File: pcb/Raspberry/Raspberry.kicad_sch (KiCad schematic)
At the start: 24 parts, among them J1 +5V, J10 SWCLK, J11 GND, J12 SWDIO, J13 UART_TX, J14 UART_RX, J15 PC1, J16 PC0, J17 PB14, J18 GND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

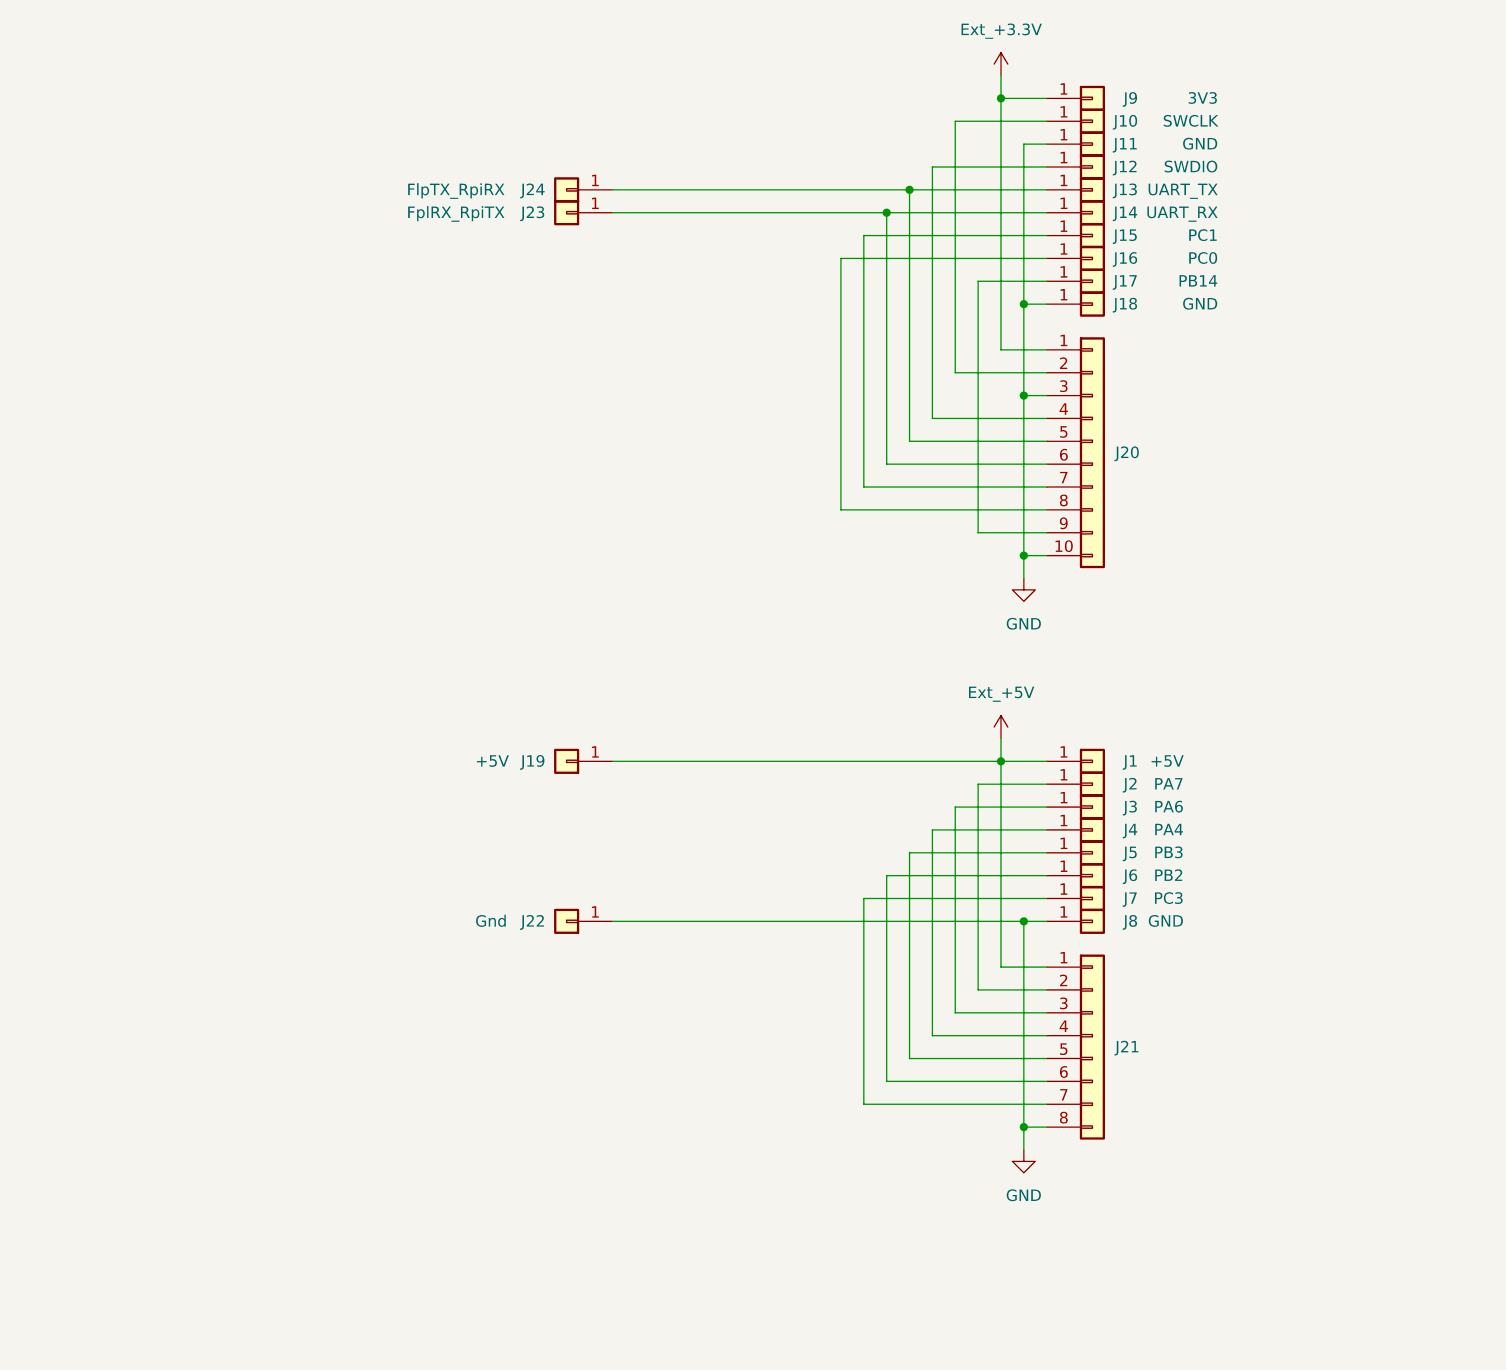
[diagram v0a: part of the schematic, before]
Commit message: [RPI] Draw schematic
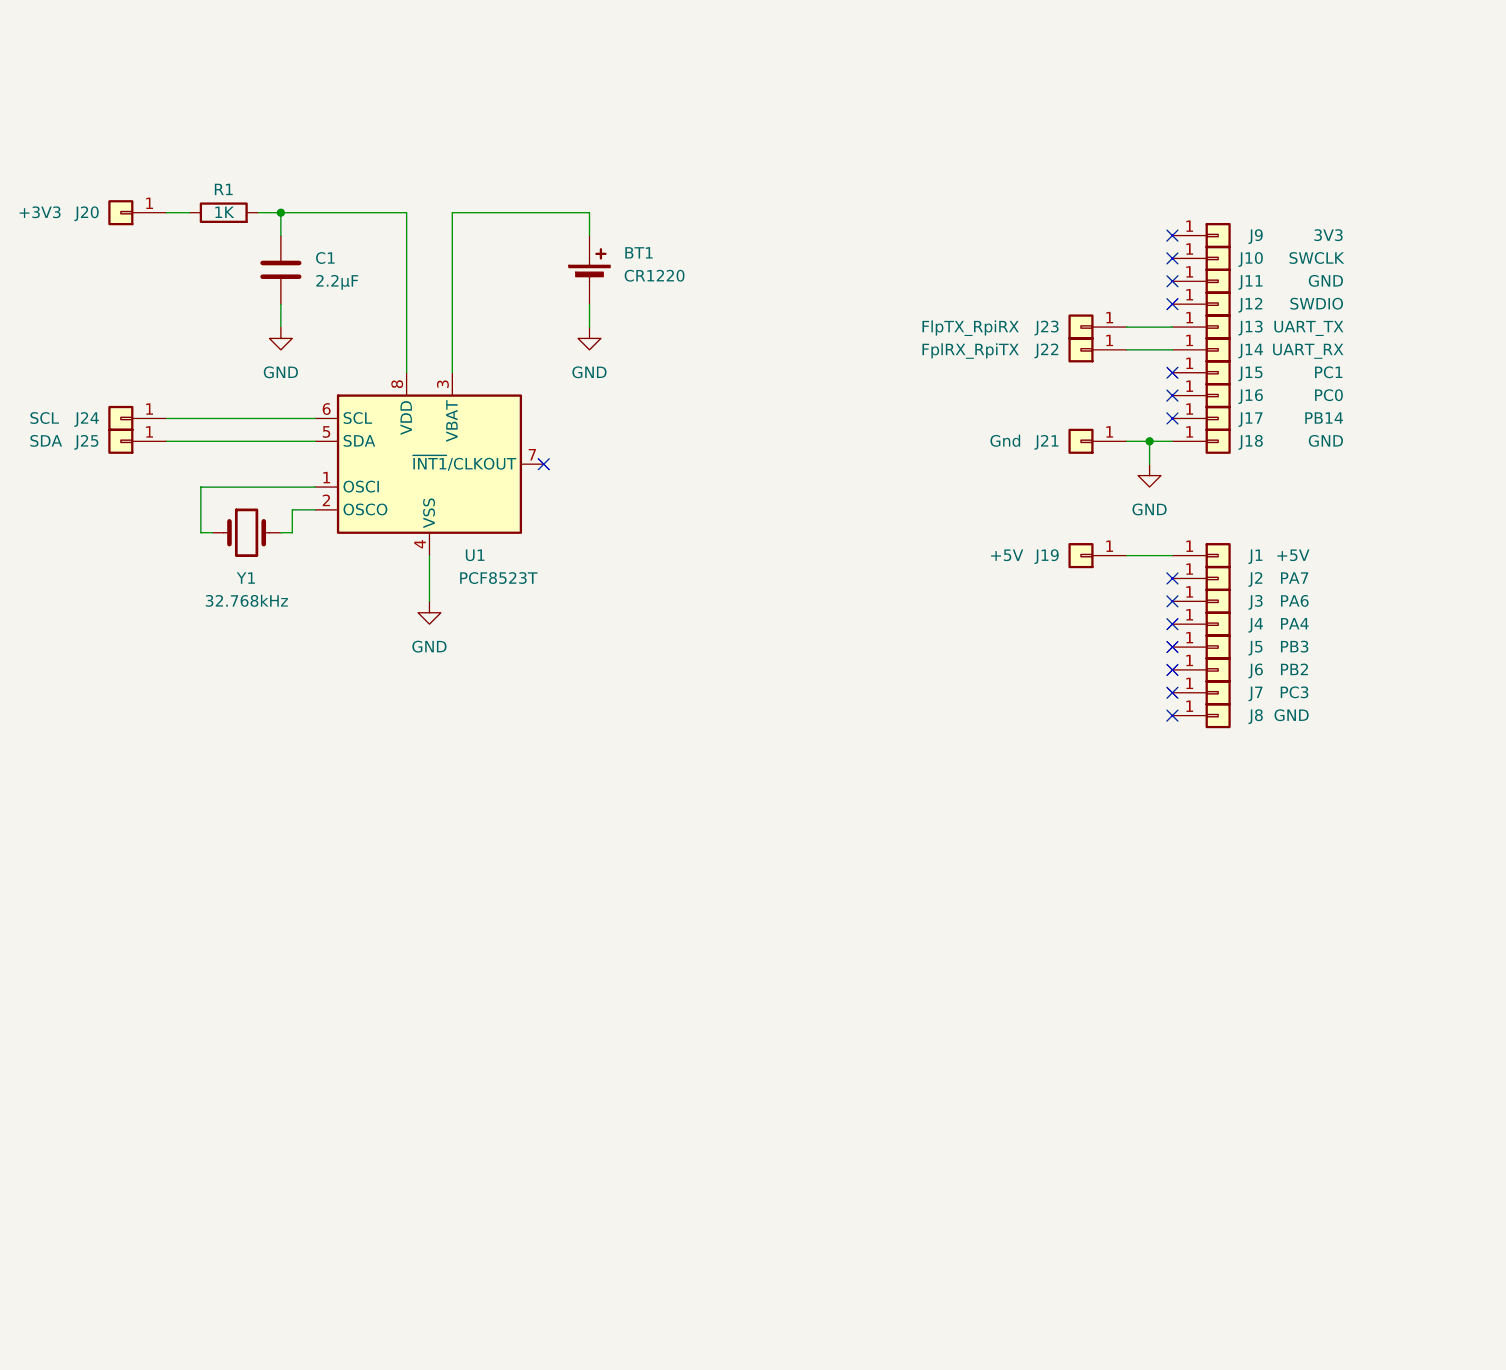
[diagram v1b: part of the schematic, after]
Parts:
- removed J20: Conn_01x10, Connector_PinHeader_2.54mm:PinHeader_1x10_P2.54mm_Vertical, symbol Connector_Generic:Conn_01x10
- removed J21: Conn_01x08, Connector_PinHeader_2.54mm:PinHeader_1x08_P2.54mm_Vertical, symbol Connector_Generic:Conn_01x08
- added BT1: CR1220, MeineBib:Q&J CR1220-2, symbol Device:Battery_Cell
- added C1: 2.2µF, Capacitor_SMD:C_0603_1608Metric, symbol Device:C
- added J20: +3V3, MeineBib:Protopin_Small, symbol Connector_Generic:Conn_01x01
- added J24: SCL, MeineBib:Protopin_Small, symbol Connector_Generic:Conn_01x01
- added J25: SDA, MeineBib:Protopin_Small, symbol Connector_Generic:Conn_01x01
- added R1: 1K, Resistor_SMD:R_0603_1608Metric, symbol Device:R
- added U1: PCF8523T, Package_SO:SOIC-8_3.9x4.9mm_P1.27mm, symbol Timer_RTC:PCF8523T
- added Y1: 32.768kHz, Crystal:Crystal_SMD_3215-2Pin_3.2x1.5mm, symbol Device:Crystal
- J1, J10, J11, J12, J13, J14, J15, J16, J17, J18, J2, J3, J4, J5, J6, J7, J8, J9: now left out of the parts list
- J19: footprint MeineBib:Board-Board-1mmEdge-2,54mm -> MeineBib:Protopin_Small; now left out of the parts list
- J21: renamed from J22; footprint MeineBib:Board-Board-1mmEdge-2,54mm -> MeineBib:Protopin_Small; now left out of the parts list
- J22: renamed from J23; footprint MeineBib:Board-Board-1mmEdge-2,54mm -> MeineBib:Protopin_Small; now left out of the parts list
- J23: renamed from J24; footprint MeineBib:Board-Board-1mmEdge-2,54mm -> MeineBib:Protopin_Small; now left out of the parts list
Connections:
- net GND: now also BT1.2 (-), C1.2, U1.4 (VSS); no longer J11.1 (Pin_1), J8.1 (Pin_1)
- net Ext_+3.3V: no longer names the net of J9.1 (Pin_1)
- net Ext_+5V: no longer names the net of J1.1 (Pin_1), J19.1 (Pin_1)
- new net: BT1.1 (+), U1.3 (VBAT)
- new net: J25.1 (Pin_1), U1.5 (SDA)
- new net: J20.1 (Pin_1), R1.1
- new net: U1.1 (OSCI), Y1.1
- new net: U1.2 (OSCO), Y1.2
- new net: J24.1 (Pin_1), U1.6 (SCL)
- new net: C1.1, R1.2, U1.8 (VDD)
- no-connect marks 0 -> 15
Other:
- moved on the sheet: J1, J10, J11, J12, J13, J14, J15, J16, J17, J18, J19, J2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

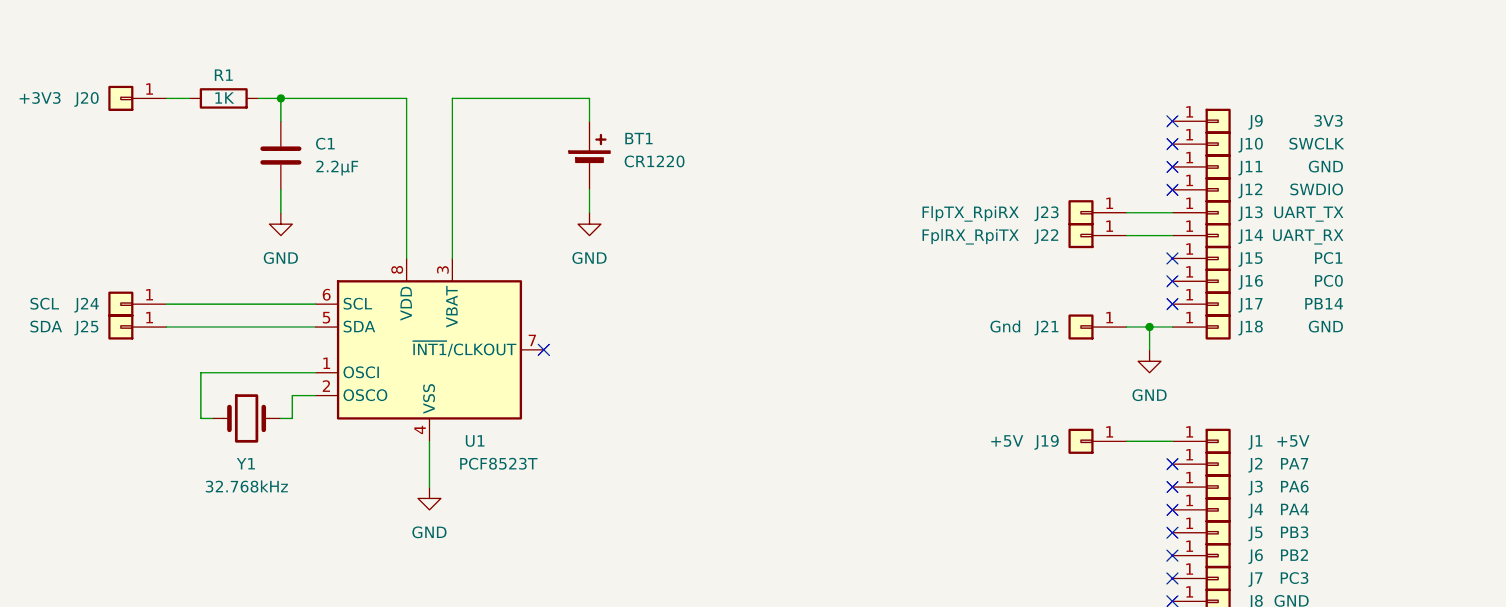
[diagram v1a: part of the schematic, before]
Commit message: [RPI] Route PCB
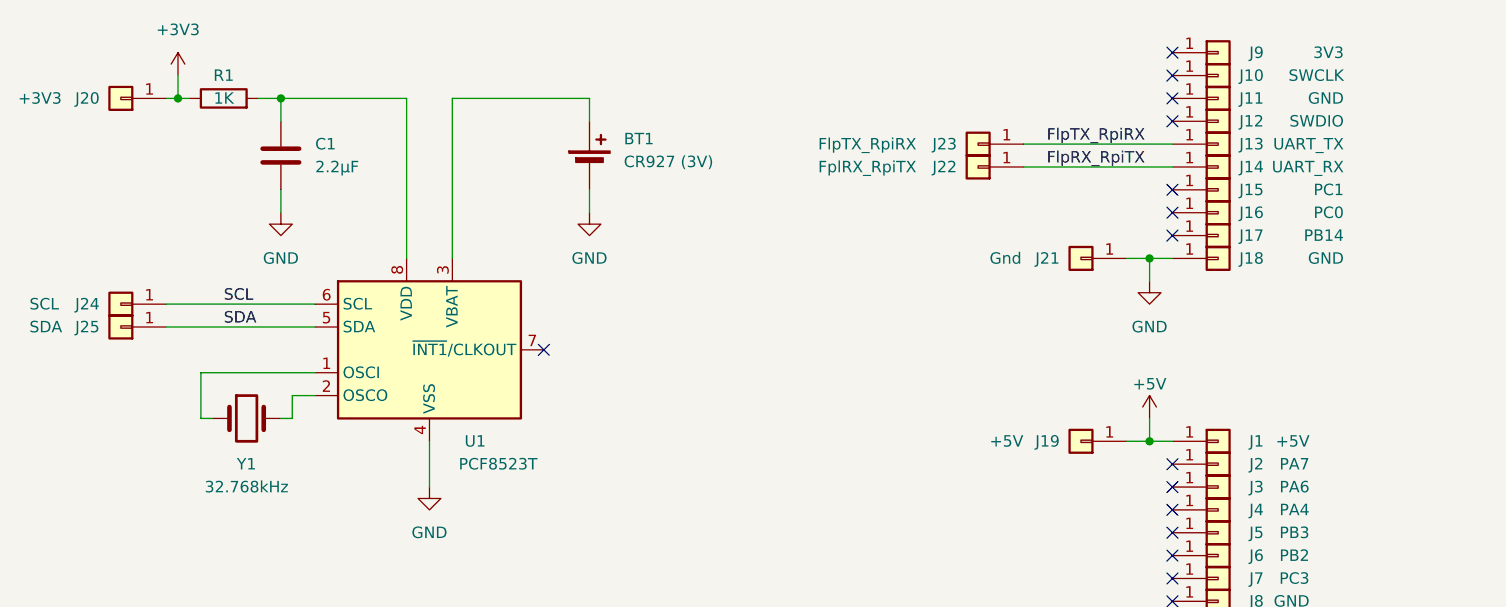
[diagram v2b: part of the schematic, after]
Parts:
- BT1: value CR1220 -> CR927 (3V); footprint MeineBib:Q&J CR1220-2 -> MeineBib:MY-927-01 CR927 Battery Holder; LCSC C70381 -> C964850
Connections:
- net FlpRX_RpiTX: now reaches J14.1 (Pin_1), J22.1 (Pin_1)
- net SDA: now reaches J25.1 (Pin_1), U1.5 (SDA)
- net +3V3: now reaches J20.1 (Pin_1), R1.1
- net SCL: now reaches J24.1 (Pin_1), U1.6 (SCL)
- net FlpTX_RpiRX: now reaches J13.1 (Pin_1), J23.1 (Pin_1)
- net +5V: now reaches J1.1 (Pin_1), J19.1 (Pin_1)
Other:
- moved on the sheet: J10, J11, J12, J13, J14, J15, J16, J17, J18, J21, J22, J23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

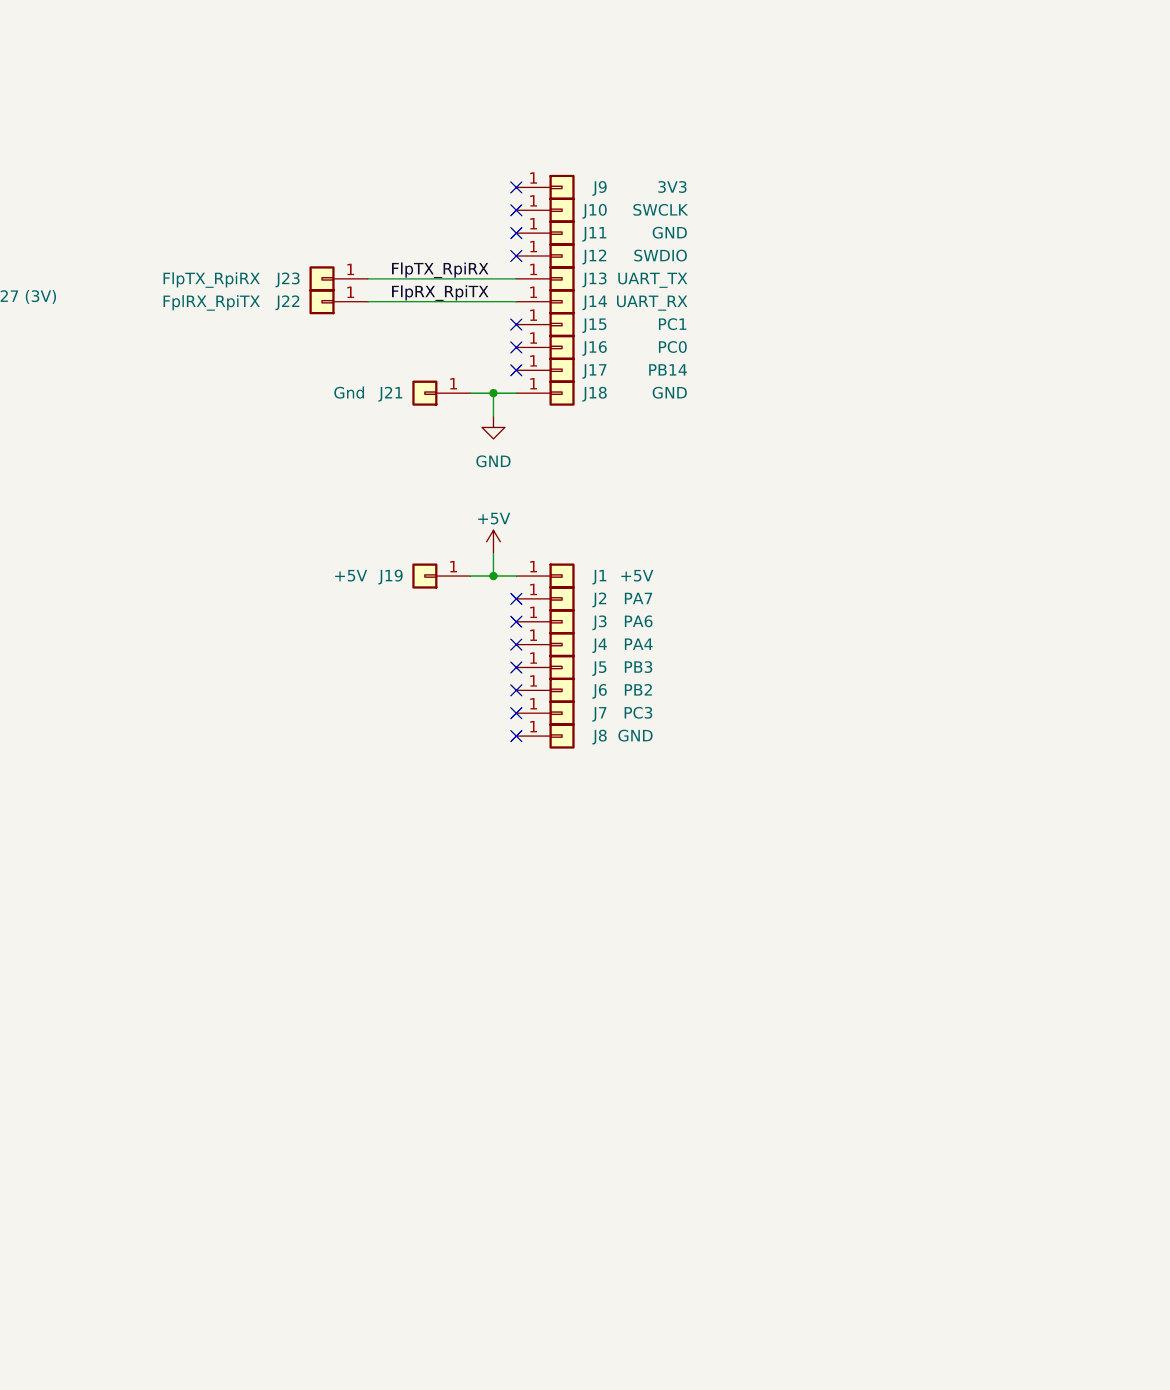
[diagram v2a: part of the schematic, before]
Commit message: [RPI] Fix PCB not actually connected to Flipper
- Added previously removed headers that act as mandatory vias from one side to the other.
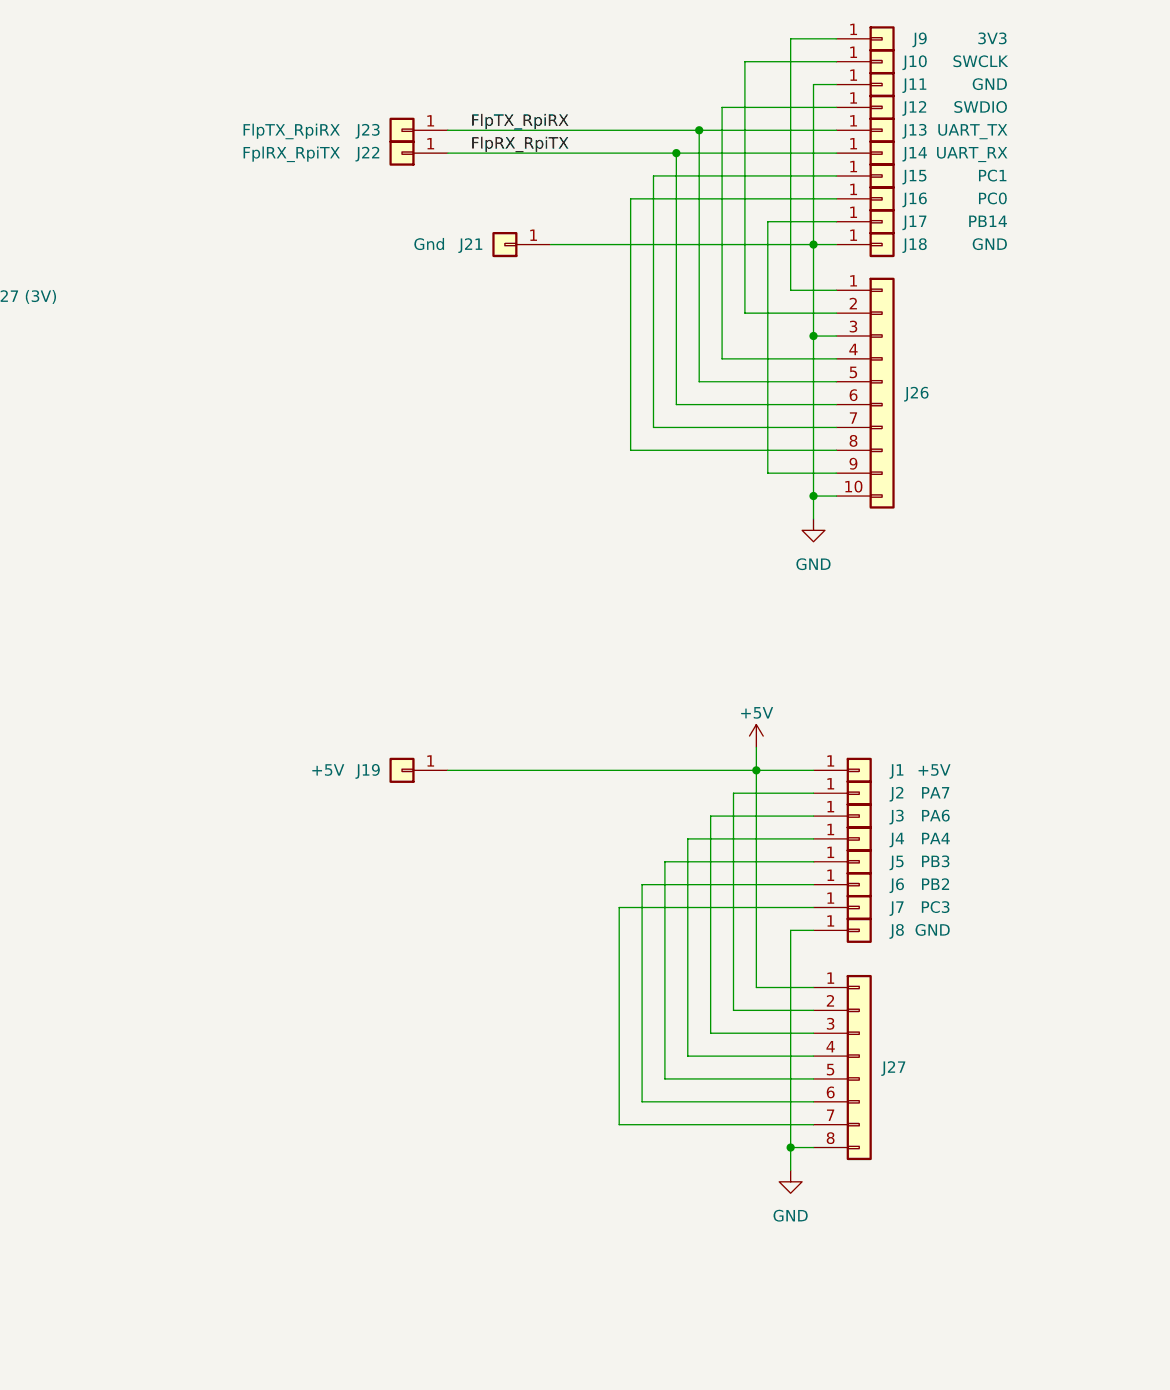
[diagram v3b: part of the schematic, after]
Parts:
- added J26: Conn_01x10, Connector_PinHeader_2.54mm:PinHeader_1x10_P2.54mm_Vertical, symbol Connector_Generic:Conn_01x10
- added J27: Conn_01x08, Connector_PinHeader_2.54mm:PinHeader_1x08_P2.54mm_Vertical, symbol Connector_Generic:Conn_01x08
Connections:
- net +5V: now also J27.1 (Pin_1)
- net FlpRX_RpiTX: now also J26.6 (Pin_6)
- net FlpTX_RpiRX: now also J26.5 (Pin_5)
- net GND: now also J11.1 (Pin_1), J8.1 (Pin_1), J26.10 (Pin_10), J26.3 (Pin_3), J27.8 (Pin_8)
- net at J17.1 (Pin_1): now also J26.9 (Pin_9)
- net at J15.1 (Pin_1): now also J26.7 (Pin_7)
- net at J10.1 (Pin_1): now also J26.2 (Pin_2)
- net at J9.1 (Pin_1): now also J26.1 (Pin_1)
- net at J6.1 (Pin_1): now also J27.6 (Pin_6)
- net at J16.1 (Pin_1): now also J26.8 (Pin_8)
- net at J2.1 (Pin_1): now also J27.2 (Pin_2)
- net at J5.1 (Pin_1): now also J27.5 (Pin_5)
- net at J12.1 (Pin_1): now also J26.4 (Pin_4)
- net at J7.1 (Pin_1): now also J27.7 (Pin_7)
- net at J3.1 (Pin_1): now also J27.3 (Pin_3)
- net at J4.1 (Pin_1): now also J27.4 (Pin_4)
- no-connect marks 15 -> 1
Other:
- moved on the sheet: J1, J10, J11, J12, J13, J14, J15, J16, J17, J18, J19, J2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
